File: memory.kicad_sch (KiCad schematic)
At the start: 43 parts, among them IC5001 MT40A1G16TB-062E_IT_F, U5001 AM6231ASGGGAALW

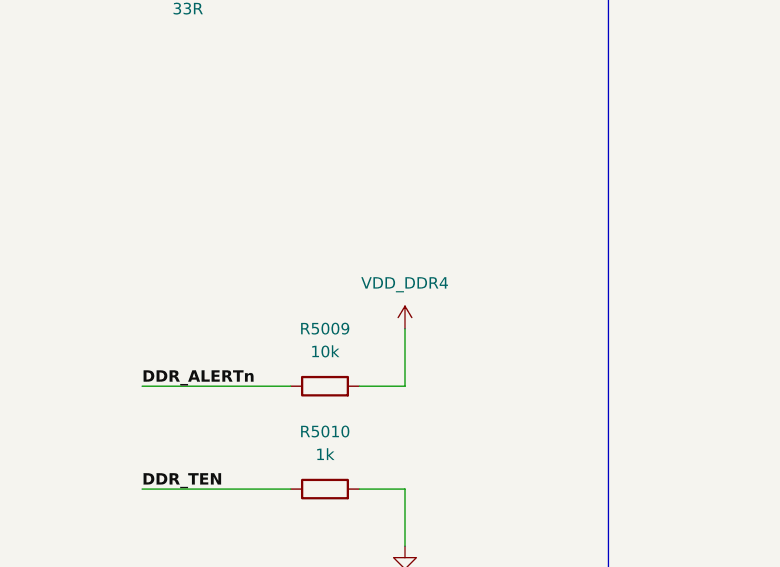
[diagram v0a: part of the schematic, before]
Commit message: Fixed more errors and warnings
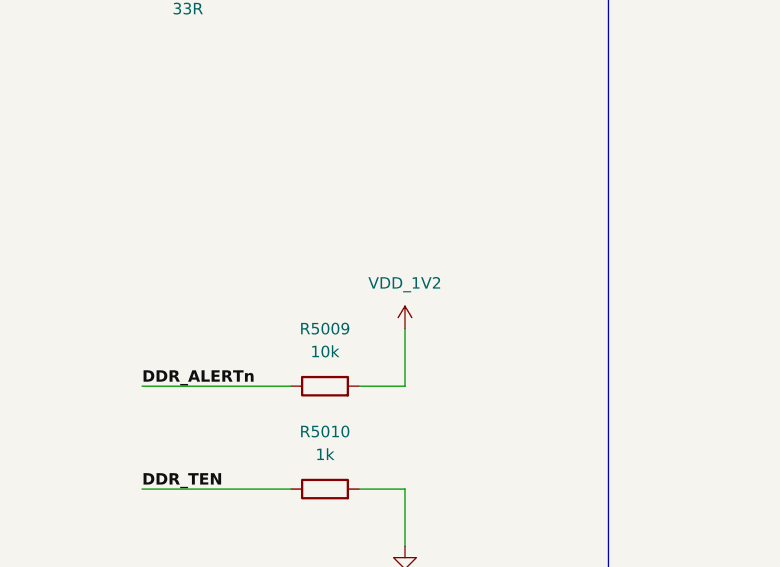
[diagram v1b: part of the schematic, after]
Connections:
- net VDD_DDR4 is gone; now on net VDD_1V2: R5009.2
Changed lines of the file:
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@@
 			)
 		)
-		(property "Value" "VDD_DDR4"
+		(property "Value" "VDD_1V2"
 			(at 554.99 194.31 0)
 			(effects

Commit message: Fixed ERC errors and warnings (zero errors and zero warnings)
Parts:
- removed U5001: AM6231ASGGGAALW, symbol SoftServicesSymbolLibrary:AM6231ASGGGAALW
- added U1001: AM6231ASGGGAALW, symbol SoftServicesSymbolLibrary:AM6231ASGGGAALW
- renumbered R5009 to R5005, R5005 to R5006, R5010 to R5008, R5006 to R5009, R5008 to R5010
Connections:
- net DDR_A0: now also U1001.J1 (DDR0_A0)
- net DDR_A1: now also U1001.J2 (DDR0_A1)
- net DDR_A10: now also U1001.R5 (DDR0_A10)
- net DDR_A11: now also U1001.P5 (DDR0_A11)
- net DDR_A12: now also U1001.R6 (DDR0_A12)
- net DDR_A13: now also U1001.R1 (DDR0_A13)
- net DDR_A14_WEn: now also U1001.N3 (DDR0_WE_N)
- net DDR_A15_CAS: now also U1001.M4 (DDR0_CAS_N)
- net DDR_A16_RAS: now also U1001.M5 (DDR0_RAS_N)
- net DDR_A2: now also U1001.K3 (DDR0_A2)
- net DDR_A3: now also U1001.L5 (DDR0_A3)
- net DDR_A4: now also U1001.K4 (DDR0_A4)
- net DDR_A5: now also U1001.K1 (DDR0_A5)
- net DDR_A6: now also U1001.R2 (DDR0_A6)
- net DDR_A7: now also U1001.P2 (DDR0_A7)
- net DDR_A8: now also U1001.P1 (DDR0_A8)
- net DDR_A9: now also U1001.P4 (DDR0_A9)
- net DDR_ACTn: now also U1001.N6 (DDR0_ACT_N)
- net DDR_ALERTn: now also U1001.R3 (DDR0_ALERT_N)
- net DDR_BA0: now also U1001.M1 (DDR0_BA0)
- net DDR_BA1: now also U1001.N1 (DDR0_BA1)
- net DDR_BG0: now also U1001.T4 (DDR0_BG0)
- net DDR_CKE: now also U1001.H2 (DDR0_CKE0)
- net DDR_CLKN: now also U1001.L2 (DDR0_CK0_N)
- net DDR_CLKP: now also U1001.L1 (DDR0_CK0)
- net DDR_CSn: now also U1001.L6 (DDR0_CS0_N)
- net DDR_DQ0: now also U1001.F4 (DDR0_DQ0)
- net DDR_DQ1: now also U1001.G5 (DDR0_DQ1)
- net DDR_DQ10: now also U1001.U2 (DDR0_DQ10)
- net DDR_DQ11: now also U1001.V5 (DDR0_DQ11)
- net DDR_DQ12: now also U1001.W2 (DDR0_DQ12)
- net DDR_DQ13: now also U1001.V6 (DDR0_DQ13)
- net DDR_DQ14: now also U1001.Y1 (DDR0_DQ14)
- net DDR_DQ15: now also U1001.W1 (DDR0_DQ15)
- net DDR_DQ2: now also U1001.F3 (DDR0_DQ2)
- net DDR_DQ3: now also U1001.H6 (DDR0_DQ3)
- net DDR_DQ4: now also U1001.E3 (DDR0_DQ4)
- net DDR_DQ5: now also U1001.G2 (DDR0_DQ5)
- net DDR_DQ6: now also U1001.F2 (DDR0_DQ6)
- net DDR_DQ7: now also U1001.F1 (DDR0_DQ7)
- net DDR_DQ8: now also U1001.U1 (DDR0_DQ8)
- net DDR_DQ9: now also U1001.U3 (DDR0_DQ9)
- net DDR_LDM: now also U1001.H5 (DDR0_DM0)
- net DDR_LDQS_N: now also U1001.E2 (DDR0_DQS0_N)
- net DDR_LDQS_P: now also U1001.E1 (DDR0_DQS0)
- net DDR_ODT: now also U1001.H1 (DDR0_ODT0)
- net DDR_PARITY: now also U1001.T1 (DDR0_PAR)
- net DDR_RESET#: now also U1001.G1 (DDR0_RESET0_N)
- net DDR_UDM: now also U1001.W5 (DDR0_DM1)
- net DDR_UDQS_N: now also U1001.V2 (DDR0_DQS1_N)
- net DDR_UDQS_P: now also U1001.V1 (DDR0_DQS1)
- net at R5007.2: now also U1001.M2 (DDR0_CAL0)

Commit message: Labeled all nets and added some footprints
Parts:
- IC5001: footprint (none) -> Package_BGA:FBGA-96_7.5x13mm_Layout9x16_P0.8mm
- U1001: footprint (none) -> AM6231ASGGGAALW:BGA425C50P25X25_1300X1300X89
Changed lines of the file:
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@@
 			)
 		)
-		(property "Footprint" ""
+		(property "Footprint" "Package_BGA:FBGA-96_7.5x13mm_Layout9x16_P0.8mm"
 			(at 309.88 177.8 0)
 			(effects
@@
 			)
 		)
-		(property "Footprint" ""
+		(property "Footprint" "AM6231ASGGGAALW:BGA425C50P25X25_1300X1300X89"
 			(at 133.35 179.07 0)
 			(effects

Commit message: Double checked power, ddr4, USB, MMC and added bootstrap. Also added buttons and added pinmuxing in sysconfig
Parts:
- removed IC5001: MT40A1G16TB-062E_IT_F, Package_BGA:FBGA-96_7.5x13mm_Layout9x16_P0.8mm, symbol SoftServicesSymbolLibrary:MT40A1G16TB-062E_IT_F
- added U5001: K4AAG165WA-BCWE, Package_BGA:FBGA-96_9x13mm_Layout9x16_P0.8mm, symbol SoftServicesSymbolLibrary:K4AAG165WA-BCWE
- C5019: value 0.01u -> 0.1u
- R5006: value 0R -> 240R
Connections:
- net DDR_A0: now also U5001.P3 (A0)
- net DDR_A1: now also U5001.P7 (A1)
- net DDR_A10: now also U5001.M3 (A10/AP)
- net DDR_A11: now also U5001.T2 (A11)
- net DDR_A12: now also U5001.M7 (A12/BC_N)
- net DDR_A13: now also U5001.T8 (A13)
- net DDR_A14_WEn: now also U5001.L2 (WE_N/A14)
- net DDR_A15_CAS: now also U5001.M8 (CAS_N/A15)
- net DDR_A16_RAS: now also U5001.L8 (RAS_N/A16)
- net DDR_A2: now also U5001.R3 (A2)
- net DDR_A3: now also U5001.N7 (A3)
- net DDR_A4: now also U5001.N3 (A4)
- net DDR_A5: now also U5001.P8 (A5)
- net DDR_A6: now also U5001.P2 (A6)
- net DDR_A7: now also U5001.R8 (A7)
- net DDR_A8: now also U5001.R2 (A8)
- net DDR_A9: now also U5001.R7 (A9)
- net DDR_ACTn: now also U5001.L3 (ACT_N)
- net DDR_ALERTn: now also U5001.P9 (ALERT_N)
- net DDR_BA0: now also U5001.N2 (BA0)
- net DDR_BA1: now also U5001.N8 (BA1)
- net DDR_BG0: now also U5001.M2 (BG0)
- net DDR_CKE: now also U5001.K2 (CKE)
- net DDR_CLKN: now also U5001.K8 (CK_C)
- net DDR_CLKP: now also U5001.K7 (CK_T)
- net DDR_CSn: now also U5001.L7 (CS_N)
- net DDR_DQ0: now also U5001.G2 (DQ0)
- net DDR_DQ1: now also U5001.F7 (DQ1)
- net DDR_DQ10: now also U5001.C3 (DQ10)
- net DDR_DQ11: now also U5001.C7 (DQ11)
- net DDR_DQ12: now also U5001.C2 (DQ12)
- net DDR_DQ13: now also U5001.C8 (DQ13)
- net DDR_DQ14: now also U5001.D3 (DQ14)
- net DDR_DQ15: now also U5001.D7 (DQ15)
- net DDR_DQ2: now also U5001.H3 (DQ2)
- net DDR_DQ3: now also U5001.H7 (DQ3)
- net DDR_DQ4: now also U5001.H2 (DQ4)
- net DDR_DQ5: now also U5001.H8 (DQ5)
- net DDR_DQ6: now also U5001.J3 (DQ6)
- net DDR_DQ7: now also U5001.J7 (DQ7)
- net DDR_DQ8: now also U5001.A3 (DQ8)
- net DDR_DQ9: now also U5001.B8 (DQ9)
- net DDR_LDM: now also U5001.E7 (NF/LDM_N/LDBI_N)
- net DDR_LDQS_N: now also U5001.F3 (LDQS_C)
- net DDR_LDQS_P: now also U5001.G3 (LDQS_T)
- net DDR_ODT: now also U5001.K3 (ODT)
- net DDR_PARITY: now also U5001.T3 (PAR)
- net DDR_RESET#: now also U5001.P1 (RESET_N)
- net DDR_TEN: now also U5001.N9 (TEN)
- net DDR_UDM: now also U5001.E2 (NF/UDM_N/UDBI_N)
- net DDR_UDQS_N: now also U5001.A7 (UDQS_C)
- net DDR_UDQS_P: now also U5001.B7 (UDQS_T)
- net DDR_VPP: now also U5001.B1 (VPP), U5001.R9 (VPP)
- net DDR_VREFCA: now also U5001.M1 (VREFCA)
- net GND: now also U5001.A2 (VSSQ), U5001.A8 (VSSQ), U5001.B2 (VSS), U5001.C9 (VSSQ), U5001.D2 (VSSQ), U5001.D8 (VSSQ), U5001.E1 (VSS), U5001.E3 (VSSQ), U5001.E8 (VSSQ), U5001.E9 (VSS), U5001.F1 (VSSQ), U5001.G8 (VSS), U5001.H1 (VSSQ), U5001.H9 (VSSQ), U5001.K1 (VSS), U5001.K9 (VSS), U5001.M9 (VSS), U5001.N1 (VSS), U5001.T1 (VSS)
- net VDD_1V2: now also U5001.A1 (VDDQ), U5001.A9 (VDDQ), U5001.B3 (VDD), U5001.B9 (VDD), U5001.C1 (VDDQ), U5001.D1 (VDD), U5001.D9 (VDDQ), U5001.F2 (VDDQ), U5001.F8 (VDDQ), U5001.G1 (VDDQ), U5001.G7 (VDD), U5001.G9 (VDDQ), U5001.J1 (VDD), U5001.J2 (VDDQ), U5001.J8 (VDDQ), U5001.J9 (VDD), U5001.L1 (VDD), U5001.L9 (VDD), U5001.R1 (VDD), U5001.T9 (VDD)
- net DDR_ZQ: now reaches R5006.1
- net DDR_ZQ: now also U5001.F9 (ZQ)
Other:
- note added: "Use bit swivelling if routing is too tough"
- moved on the sheet: R5006

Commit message: Added capcitor footprints
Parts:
- C5001: footprint (none) -> Capacitor_SMD:C_0402_1005Metric
- C5002, C5003, C5004, C5006, C5007, C5008, C5009, C5010, C5011, C5012, C5013, C5014, C5015, C5016, C5017, C5018, C5019, C5020, C5021, C5022, C5023, C5024, C5025, C5026, C5027, C5028, C5029, C5030: footprint (none) -> Capacitor_SMD:C_0201_0603Metric
- C5005: footprint (none) -> Capacitor_SMD:C_0603_1608Metric
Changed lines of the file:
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@@
 			)
 		)
-		(property "Footprint" ""
+		(property "Footprint" "Capacitor_SMD:C_0201_0603Metric"
 			(at 445.4652 288.29 0)
 			(effects
@@
 			)
 		)
-		(property "Footprint" ""
+		(property "Footprint" "Capacitor_SMD:C_0201_0603Metric"
 			(at 430.2252 189.23 0)
 			(effects
@@
 			)
 		)
-		(property "Footprint" ""
+		(property "Footprint" "Capacitor_SMD:C_0201_0603Metric"
 			(at 442.9252 157.48 0)
 			(effects
@@
 			)
 		)
-		(property "Footprint" ""
+		(property "Footprint" "Capacitor_SMD:C_0201_0603Metric"
 			(at 481.0252 189.23 0)
 			(effects
@@
 			)
 		)
-		(property "Footprint" ""
+		(property "Footprint" "Capacitor_SMD:C_0201_0603Metric"
 			(at 458.1652 288.29 0)
 			(effects
@@
 			)
 		)
-		(property "Footprint" ""
+		(property "Footprint" "Capacitor_SMD:C_0201_0603Metric"
 			(at 481.0252 157.48 0)
 			(effects
@@
 			)
 		)
-		(property "Footprint" ""
+		(property "Footprint" "Capacitor_SMD:C_0402_1005Metric"
 			(at 417.5252 128.27 0)
 			(effects
@@
 			)
 		)
-		(property "Footprint" ""
+		(property "Footprint" "Capacitor_SMD:C_0201_0603Metric"
 			(at 515.62 151.4348 0)
 			(effects
@@
 			)
 		)
-		(property "Footprint" ""
+		(property "Footprint" "Capacitor_SMD:C_0201_0603Metric"
 			(at 442.9252 128.27 0)
 			(effects
@@
 			)
 		)
-		(property "Footprint" ""
+		(property "Footprint" "Capacitor_SMD:C_0201_0603Metric"
 			(at 470.8652 288.29 0)
 			(effects
@@
 			)
 		)
-		(property "Footprint" ""
+		(property "Footprint" "Capacitor_SMD:C_0201_0603Metric"
 			(at 493.7252 189.23 0)
 			(effects
@@
 			)
 		)
-		(property "Footprint" ""
+		(property "Footprint" "Capacitor_SMD:C_0603_1608Metric"
 			(at 417.5252 157.48 0)
 			(effects
@@
 			)
 		)
-		(property "Footprint" ""
+		(property "Footprint" "Capacitor_SMD:C_0201_0603Metric"
 			(at 496.2652 288.29 0)
 			(effects
@@
 			)
 		)
-		(property "Footprint" ""
+		(property "Footprint" "Capacitor_SMD:C_0201_0603Metric"
 			(at 455.6252 157.48 0)
 			(effects
@@
 			)
 		)
-		(property "Footprint" ""
+		(property "Footprint" "Capacitor_SMD:C_0201_0603Metric"
 			(at 417.5252 189.23 0)
 			(effects
@@
 			)
 		)
-		(property "Footprint" ""
+		(property "Footprint" "Capacitor_SMD:C_0201_0603Metric"
 			(at 455.6252 189.23 0)
 			(effects
@@
 			)
 		)
-		(property "Footprint" ""
+		(property "Footprint" "Capacitor_SMD:C_0201_0603Metric"
 			(at 432.7652 288.29 0)
 			(effects
@@
 			)
 		)
-		(property "Footprint" ""
+		(property "Footprint" "Capacitor_SMD:C_0201_0603Metric"
 			(at 493.7252 220.98 0)
 			(effects
@@
 			)
 		)
-		(property "Footprint" ""
+		(property "Footprint" "Capacitor_SMD:C_0201_0603Metric"
 			(at 534.3652 288.29 0)
 			(effects
@@
 			)
 		)
-		(property "Footprint" ""
+		(property "Footprint" "Capacitor_SMD:C_0201_0603Metric"
 			(at 442.9252 189.23 0)
 			(effects
@@
 			)
 		)
-		(property "Footprint" ""
+		(property "Footprint" "Capacitor_SMD:C_0201_0603Metric"
 			(at 521.6652 288.29 0)
 			(effects
@@
 			)
 		)
-		(property "Footprint" ""
+		(property "Footprint" "Capacitor_SMD:C_0201_0603Metric"
 			(at 468.3252 157.48 0)
 			(effects
@@
 			)
 		)
-		(property "Footprint" ""
+		(property "Footprint" "Capacitor_SMD:C_0201_0603Metric"
 			(at 462.28 211.1248 0)
 			(effects
@@
 			)
 		)
-		(property "Footprint" ""
+		(property "Footprint" "Capacitor_SMD:C_0201_0603Metric"
 			(at 508.9652 288.29 0)
 			(effects
@@
 			)
 		)
-		(property "Footprint" ""
+		(property "Footprint" "Capacitor_SMD:C_0201_0603Metric"
 			(at 468.3252 189.23 0)
 			(effects
@@
 			)
 		)
-		(property "Footprint" ""
+		(property "Footprint" "Capacitor_SMD:C_0201_0603Metric"
 			(at 418.7952 234.95 0)
 			(effects
@@
 			)
 		)
-		(property "Footprint" ""
+		(property "Footprint" "Capacitor_SMD:C_0201_0603Metric"
 			(at 483.5652 288.29 0)
 			(effects
@@
 			)
 		)
-		(property "Footprint" ""
+		(property "Footprint" "Capacitor_SMD:C_0201_0603Metric"
 			(at 430.2252 157.48 0)
 			(effects
@@
 			)
 		)
-		(property "Footprint" ""
+		(property "Footprint" "Capacitor_SMD:C_0201_0603Metric"
 			(at 431.4952 234.95 0)
 			(effects
@@
 			)
 		)
-		(property "Footprint" ""
+		(property "Footprint" "Capacitor_SMD:C_0201_0603Metric"
 			(at 430.2252 128.27 0)
 			(effects

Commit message: Added almost all passive component footprints
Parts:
- FB5001, R5003, R5004, R5005, R5006, R5007, R5008, R5009, R5010: footprint (none) -> Resistor_SMD:R_0402_1005Metric
- R5001, R5002: footprint (none) -> Resistor_SMD:R_0201_0603Metric
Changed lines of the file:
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@@
 			)
 		)
-		(property "Footprint" ""
+		(property "Footprint" "Resistor_SMD:R_0402_1005Metric"
 			(at 63.5 218.948 90)
 			(effects
@@
 			)
 		)
-		(property "Footprint" ""
+		(property "Footprint" "Resistor_SMD:R_0402_1005Metric"
 			(at 546.1 218.948 90)
 			(effects
@@
 			)
 		)
-		(property "Footprint" ""
+		(property "Footprint" "Resistor_SMD:R_0201_0603Metric"
 			(at 530.86 154.178 90)
 			(effects
@@
 			)
 		)
-		(property "Footprint" ""
+		(property "Footprint" "Resistor_SMD:R_0402_1005Metric"
 			(at 440.182 231.14 90)
 			(effects
@@
 			)
 		)
-		(property "Footprint" ""
+		(property "Footprint" "Resistor_SMD:R_0201_0603Metric"
 			(at 530.86 159.258 90)
 			(effects
@@
 			)
 		)
-		(property "Footprint" ""
+		(property "Footprint" "Resistor_SMD:R_0402_1005Metric"
 			(at 458.47 224.028 90)
 			(effects
@@
 			)
 		)
-		(property "Footprint" ""
+		(property "Footprint" "Resistor_SMD:R_0402_1005Metric"
 			(at 374.65 208.788 90)
 			(effects
@@
 			)
 		)
-		(property "Footprint" ""
+		(property "Footprint" "Resistor_SMD:R_0402_1005Metric"
 			(at 520.7 128.778 90)
 			(effects
@@
 			)
 		)
-		(property "Footprint" ""
+		(property "Footprint" "Resistor_SMD:R_0402_1005Metric"
 			(at 35.052 184.15 90)
 			(effects
@@
 			)
 		)
-		(property "Footprint" ""
+		(property "Footprint" "Resistor_SMD:R_0402_1005Metric"
 			(at 546.1 207.518 90)
 			(effects
@@
 			)
 		)
-		(property "Footprint" ""
+		(property "Footprint" "Resistor_SMD:R_0402_1005Metric"
 			(at 35.052 198.12 90)
 			(effects

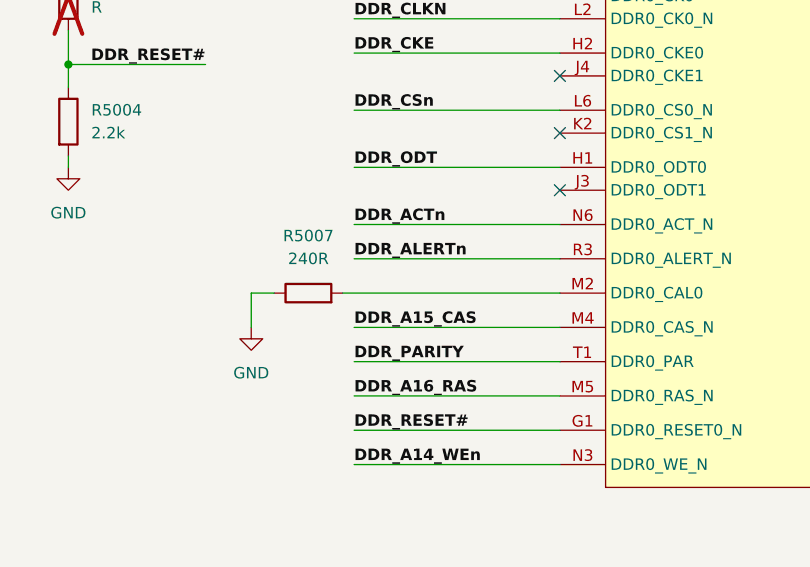
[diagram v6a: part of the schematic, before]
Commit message: Added net classes and colouring on layout editor
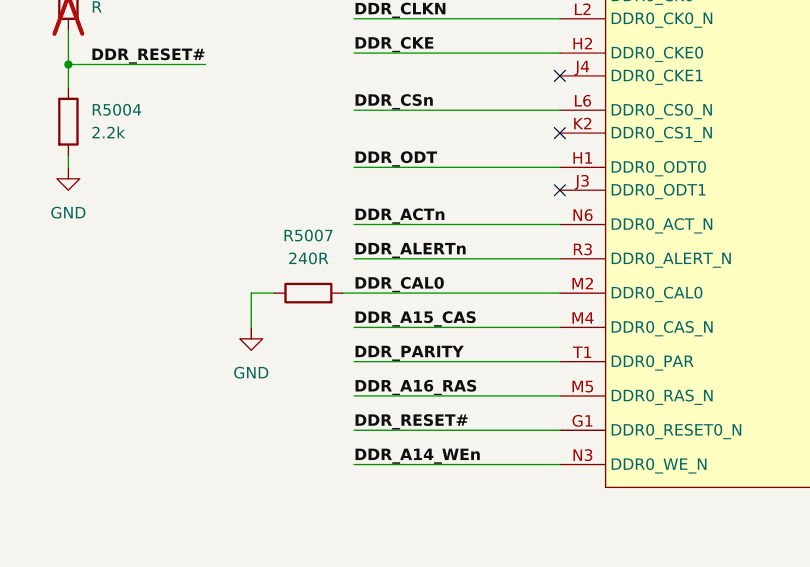
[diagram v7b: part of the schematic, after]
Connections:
- net DDR_CAL0: now reaches R5007.2, U1001.M2 (DDR0_CAL0)
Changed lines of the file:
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@@
+		)
+	)
+	(label "DDR_CAL0"
+		(at 68.58 217.17 0)
+		(effects
+			(font
+				(size 1.27 1.27)
+				(thickness 0.254)
+				(bold yes)
+			)
+			(justify left bottom)
 		)
 	)

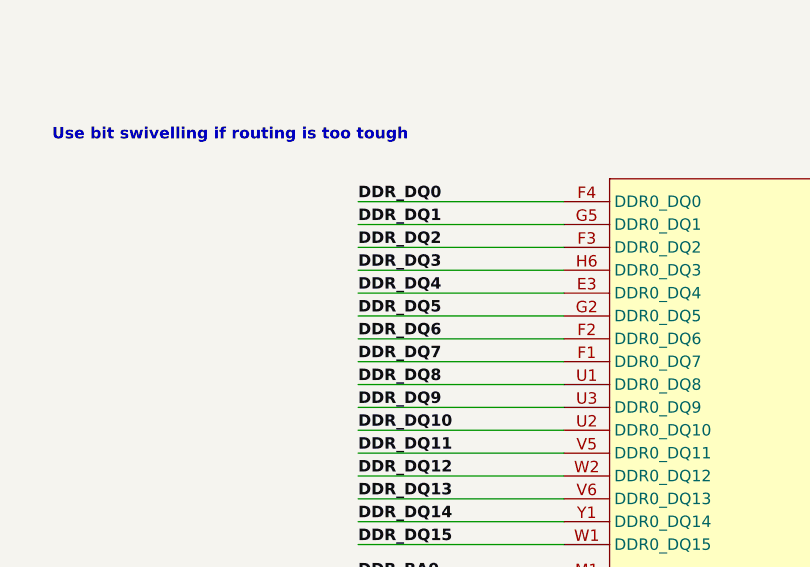
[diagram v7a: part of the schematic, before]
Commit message: Did byte swapping on DDR for easier routing
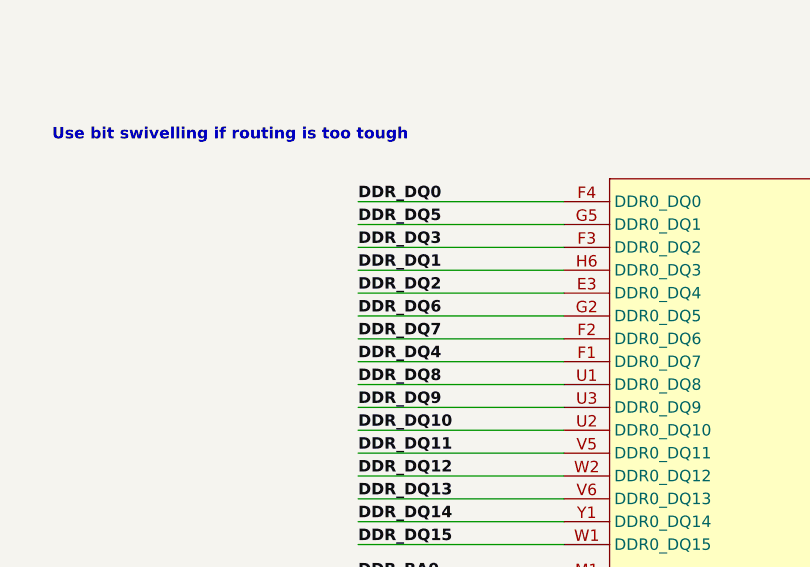
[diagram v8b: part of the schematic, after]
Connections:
- net DDR_DQ1: now also U1001.H6 (DDR0_DQ3); no longer U1001.G5 (DDR0_DQ1)
- net DDR_DQ2: now also U1001.E3 (DDR0_DQ4); no longer U1001.F3 (DDR0_DQ2)
- net DDR_DQ3: now also U1001.F3 (DDR0_DQ2); no longer U1001.H6 (DDR0_DQ3)
- net DDR_DQ4: now also U1001.F1 (DDR0_DQ7); no longer U1001.E3 (DDR0_DQ4)
- net DDR_DQ5: now also U1001.G5 (DDR0_DQ1); no longer U1001.G2 (DDR0_DQ5)
- net DDR_DQ6: now also U1001.G2 (DDR0_DQ5); no longer U1001.F2 (DDR0_DQ6)
- net DDR_DQ7: now also U1001.F2 (DDR0_DQ6); no longer U1001.F1 (DDR0_DQ7)
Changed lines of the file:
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@@
 		)
 	)
-	(label "DDR_DQ5"
+	(label "DDR_DQ6"
 		(at 68.58 135.89 0)
 		(effects
@@
 		)
 	)
-	(label "DDR_DQ7"
+	(label "DDR_DQ4"
 		(at 68.58 140.97 0)
 		(effects
@@
 		)
 	)
-	(label "DDR_DQ4"
+	(label "DDR_DQ2"
 		(at 68.58 133.35 0)
 		(effects
@@
 		)
 	)
-	(label "DDR_DQ2"
+	(label "DDR_DQ3"
 		(at 68.58 128.27 0)
 		(effects
@@
 		)
 	)
-	(label "DDR_DQ6"
+	(label "DDR_DQ7"
 		(at 68.58 138.43 0)
 		(effects
@@
 		)
 	)
-	(label "DDR_DQ1"
+	(label "DDR_DQ5"
 		(at 68.58 125.73 0)
 		(effects
@@
 		)
 	)
-	(label "DDR_DQ3"
+	(label "DDR_DQ1"
 		(at 68.58 130.81 0)
 		(effects
